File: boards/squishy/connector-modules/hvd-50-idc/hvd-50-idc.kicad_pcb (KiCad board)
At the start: 6 copper layers, 75 x 34 mm, 18 parts, among them J1 SCSI PHY Mezz, J2 Conn_02x25_Odd_Even, J3 Conn_01x04, U1 M24C02-RMC

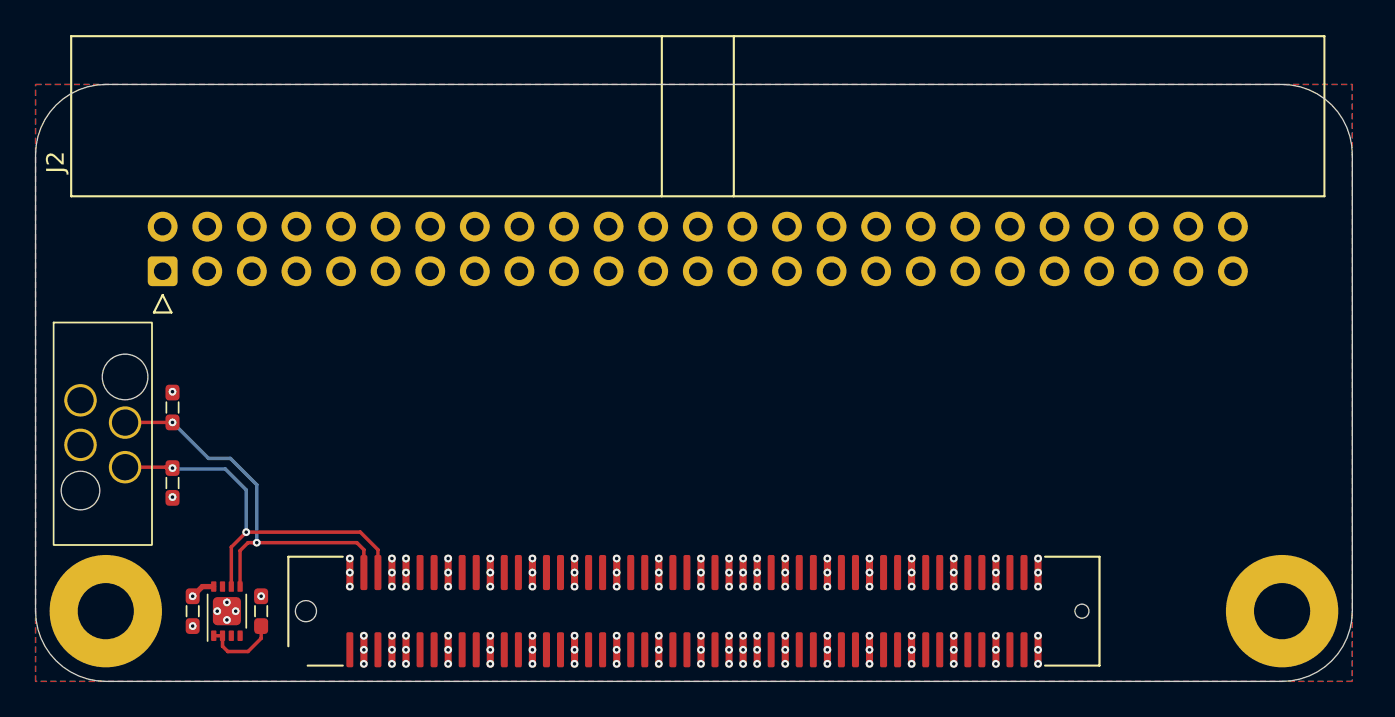
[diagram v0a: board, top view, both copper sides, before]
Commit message: squishy: connectors: routed the hvd-50-idc connector
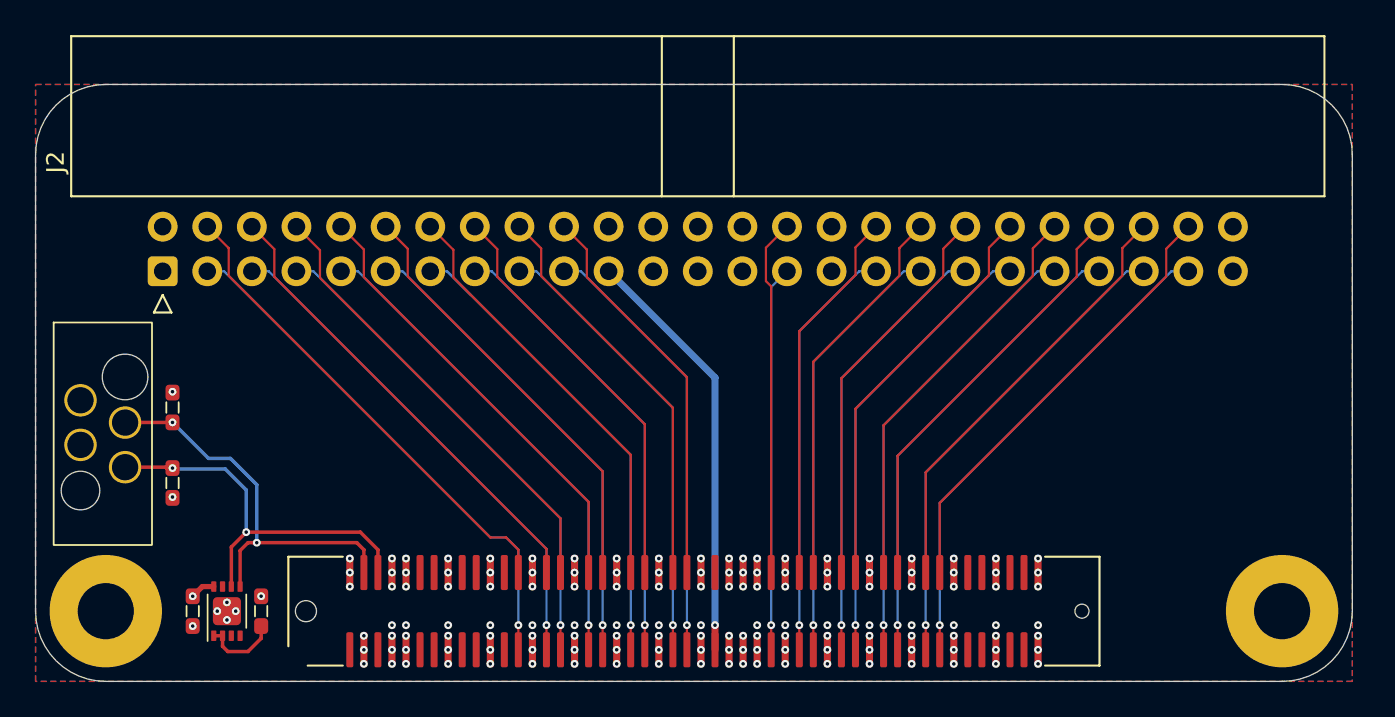
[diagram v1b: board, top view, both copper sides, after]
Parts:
- moved REF** 0.30 mm to (110.0, 131.0)
- moved REF** 0.30 mm to (110.0, 115.0)
- moved REF** 0.25 mm to (121.0, 106.0)
- moved REF** 0.25 mm to (185.0, 131.0)
- moved REF** 0.25 mm to (174.0, 140.0)
- moved REF** 0.25 mm to (174.0, 106.0)
- moved REF** 0.25 mm to (185.0, 115.0)
- moved REF** 0.25 mm to (121.0, 140.0)
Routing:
- net /CON.DB0+: track 0.00 -> 30.0 mm, vias 0 -> 1
- net /CON.DB1+: track 0.00 -> 29.1 mm, vias 0 -> 1
- net /CON.DB5+: track 0.00 -> 28.8 mm, vias 0 -> 1
- net /CON.DB2+: track 0.00 -> 28.4 mm, vias 0 -> 1
- net /CON.I/O+: track 0.00 -> 28.0 mm, vias 0 -> 1
- net /CON.DB3+: track 0.00 -> 28.0 mm, vias 0 -> 1
- net /CON.DB0-: track 0.00 -> 27.6 mm
- net /CON.REQ+: track 0.00 -> 27.3 mm, vias 0 -> 1
- net /CON.DB4+: track 0.00 -> 27.2 mm, vias 0 -> 1
- net /CON.C/D+: track 0.00 -> 26.9 mm, vias 0 -> 1
- net /CON.DB1-: track 0.00 -> 26.7 mm
- net /CON.DB7+: track 0.00 -> 26.6 mm, vias 0 -> 1
- net /CON.SEL+: track 0.00 -> 26.2 mm, vias 0 -> 1
- net /CON.DB6+: track 0.00 -> 26.1 mm, vias 0 -> 1
- net /CON.DB2-: track 0.00 -> 25.9 mm
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
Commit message: squishy: connectors: length-matched hvd-50-idc
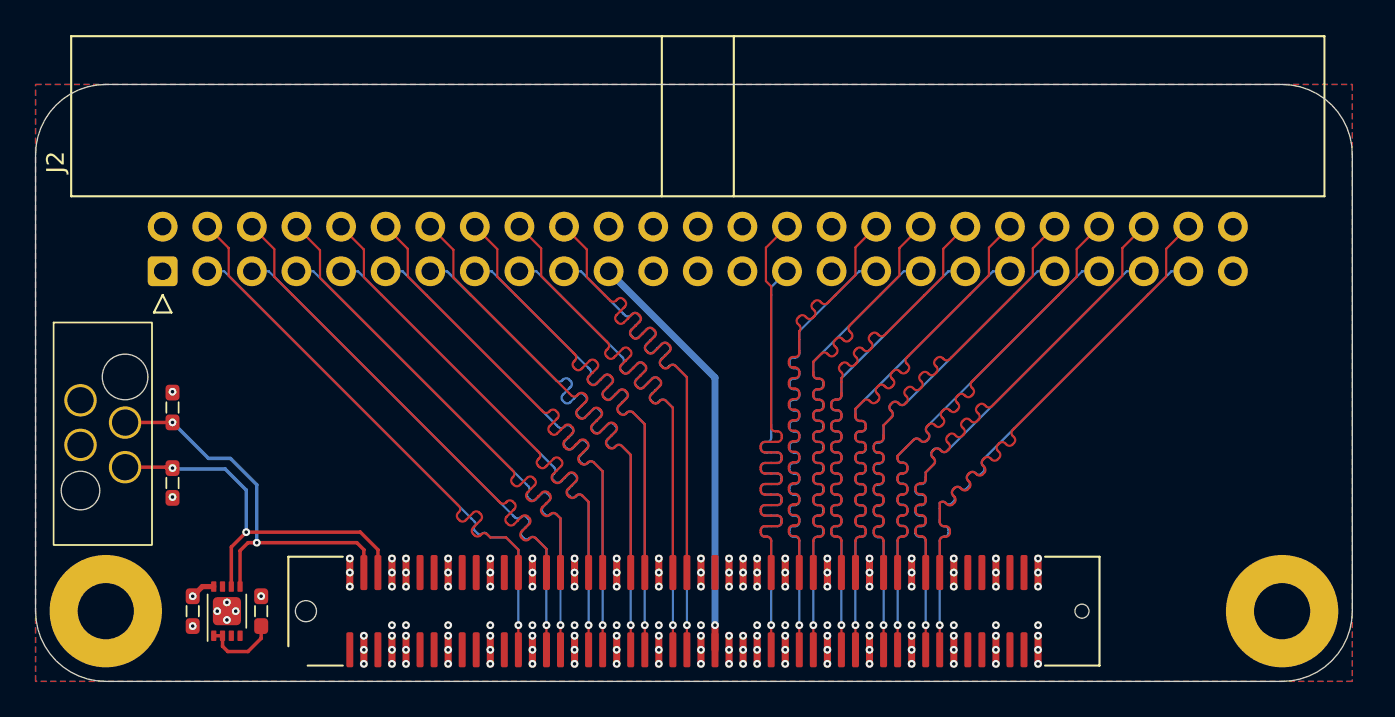
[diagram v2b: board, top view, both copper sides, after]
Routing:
- net /CON.ATN-: track 20.3 -> 29.8 mm
- net /CON.ATN+: track 21.9 -> 30.2 mm
- net /CON.BSY-: track 21.5 -> 29.6 mm
- net /CON.ACK-: track 22.2 -> 29.7 mm
- net /CON.DP0-: track 22.6 -> 29.9 mm
- net /CON.RST-: track 22.6 -> 29.7 mm
- net /CON.DB5+: track 28.8 -> 35.6 mm
- net /CON.DB7-: track 23.3 -> 29.9 mm
- net /CON.MSG-: track 23.3 -> 29.7 mm
- net /CON.DB6-: track 23.7 -> 29.9 mm
- net /CON.BSY+: track 23.9 -> 30.0 mm
- net /CON.SEL-: track 23.7 -> 29.7 mm
- net /CON.DB5-: track 24.4 -> 29.9 mm
- net /CON.ACK+: track 24.7 -> 30.1 mm
- net /CON.C/D-: track 24.5 -> 29.7 mm
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
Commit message: squishy: connectors: cleaned DRC for hvd-50-idc
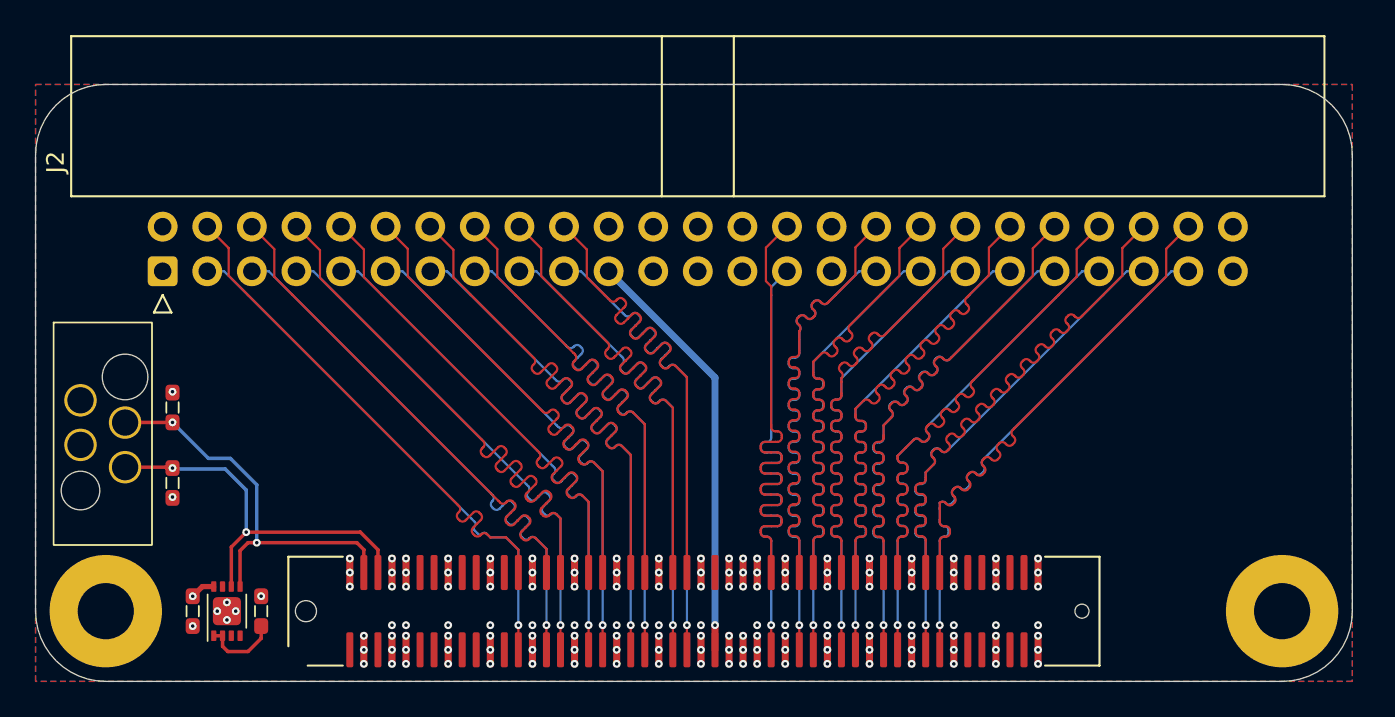
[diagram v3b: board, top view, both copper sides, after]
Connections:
- net /CON.DP12+ renamed /CON.DB12+
- net /CON.DP12- renamed /CON.DB12-
- net /CON.DP14+ renamed /CON.DB14+
- net /CON.DP14- renamed /CON.DB14-
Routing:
- net /CON.DB2-: track 29.9 -> 34.3 mm
- net /CON.DB5-: track 29.9 -> 34.2 mm
- net /CON.REQ-: track 29.8 -> 33.9 mm
- net /CON.MSG-: track 29.7 -> 33.1 mm
- net /CON.DB1+: track 30.3 -> 32.8 mm
- net /CON.DB6+: track 30.3 -> 32.8 mm
- net /CON.SEL+: track 30.2 -> 32.6 mm
- net /CON.BSY+: track 30.0 -> 32.2 mm

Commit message: squishy: connectors: Added silkscreen and layer markers to the HVD connector interface boards
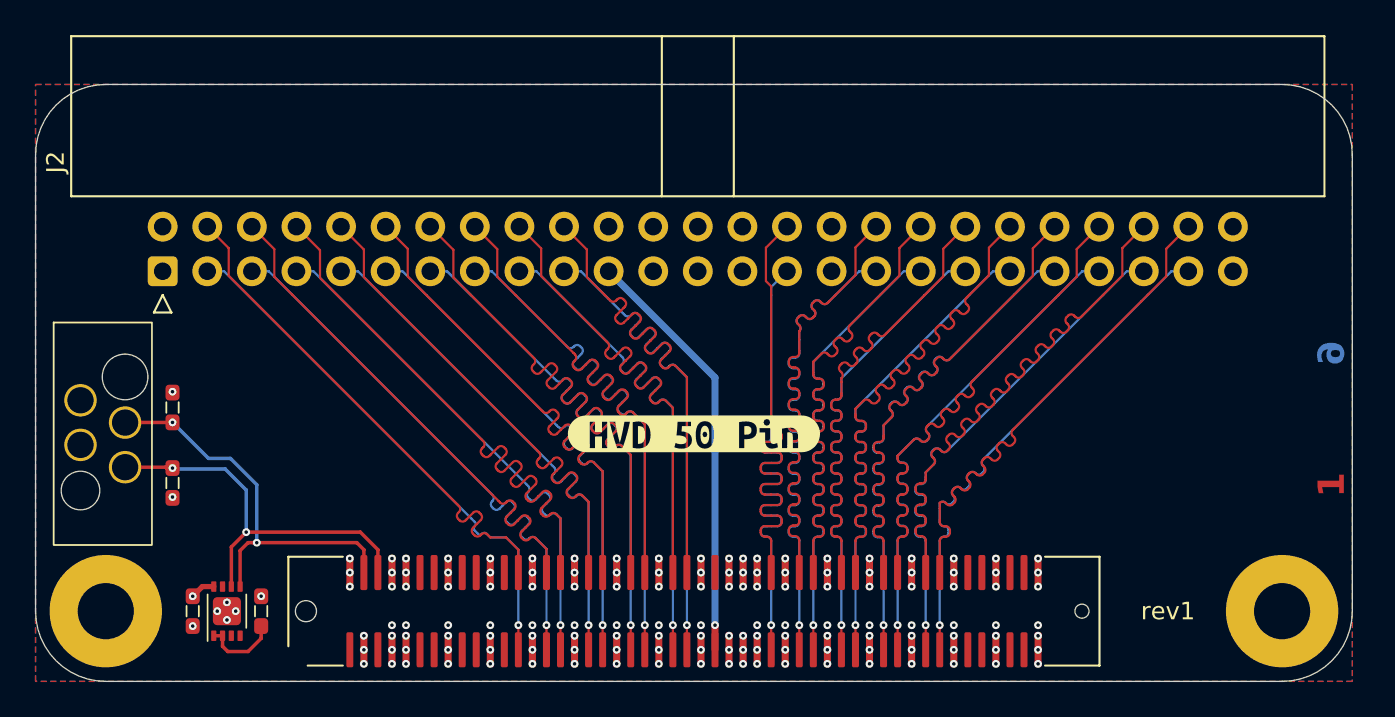
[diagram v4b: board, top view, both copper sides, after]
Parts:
- added kibuzzard-672C6174: G***, kibuzzard-672C6174, F.Cu at (147.5, 125.9)
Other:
- board text added: "1"
- board text added: "2"
- board text added: "3"
- board text added: "4"
- board text added: "5"
- board text added: "6"
- board text added: "rev1"
